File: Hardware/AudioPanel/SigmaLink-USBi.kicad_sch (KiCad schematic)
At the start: 33 parts, among them J28 Program, J32 Target, U68 74LVC2G66, U70 TPS2051B, U71 24LC512, U72 MAX809, U73 CY7C68013A-56, Y9 24MHz

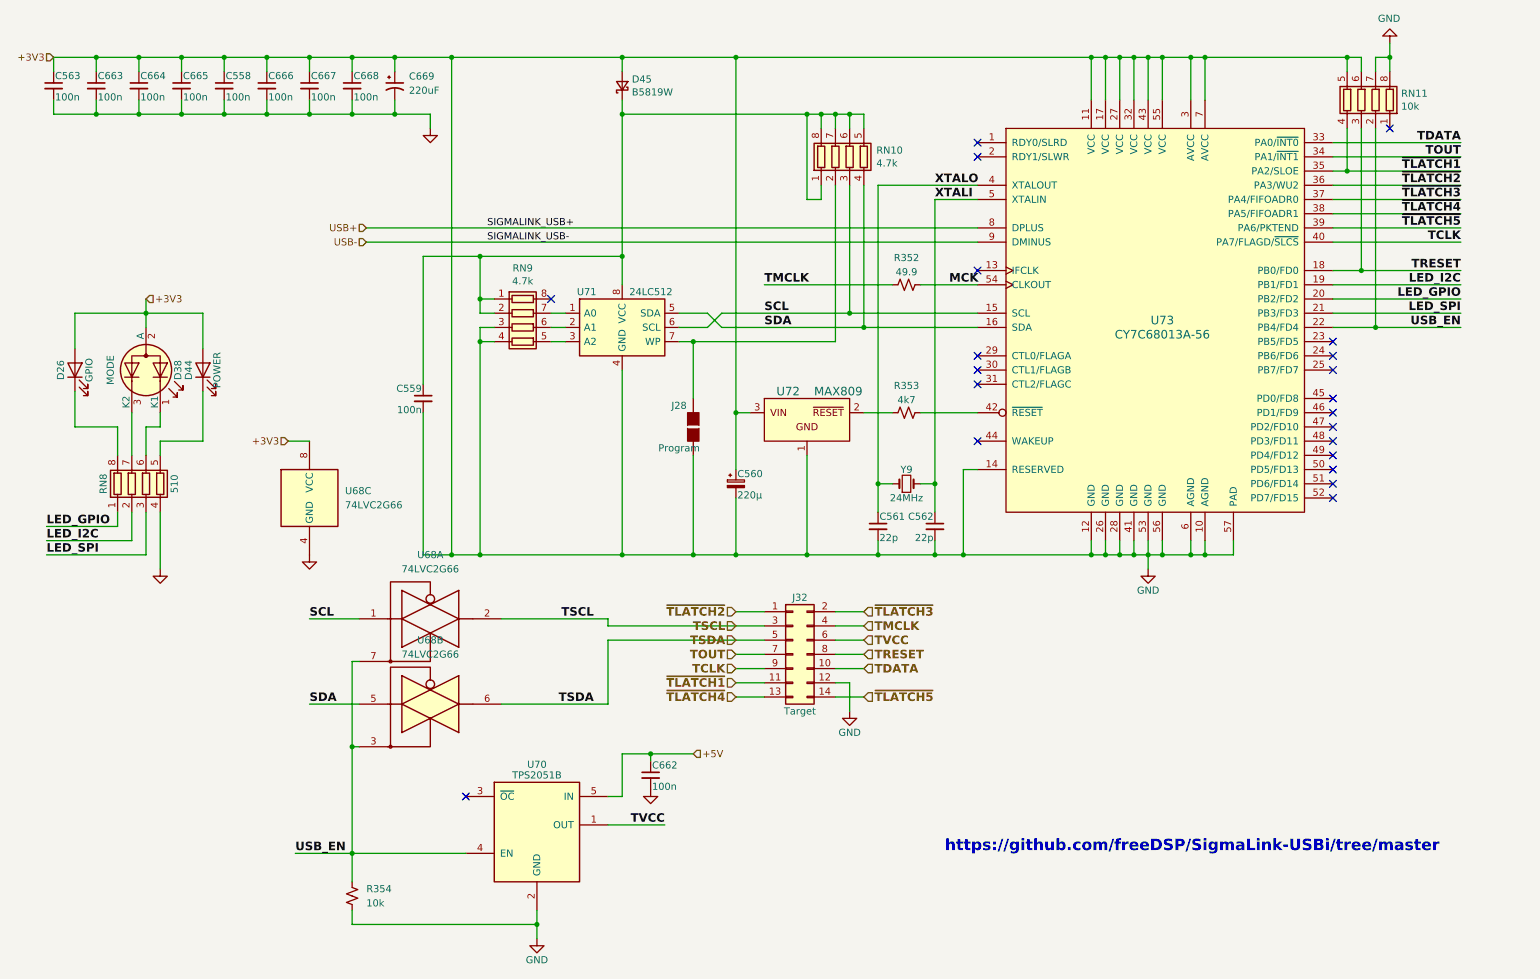
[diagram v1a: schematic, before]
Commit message: Realized that I need to rethink how I'm going to mix the radio audio with the stereo audio
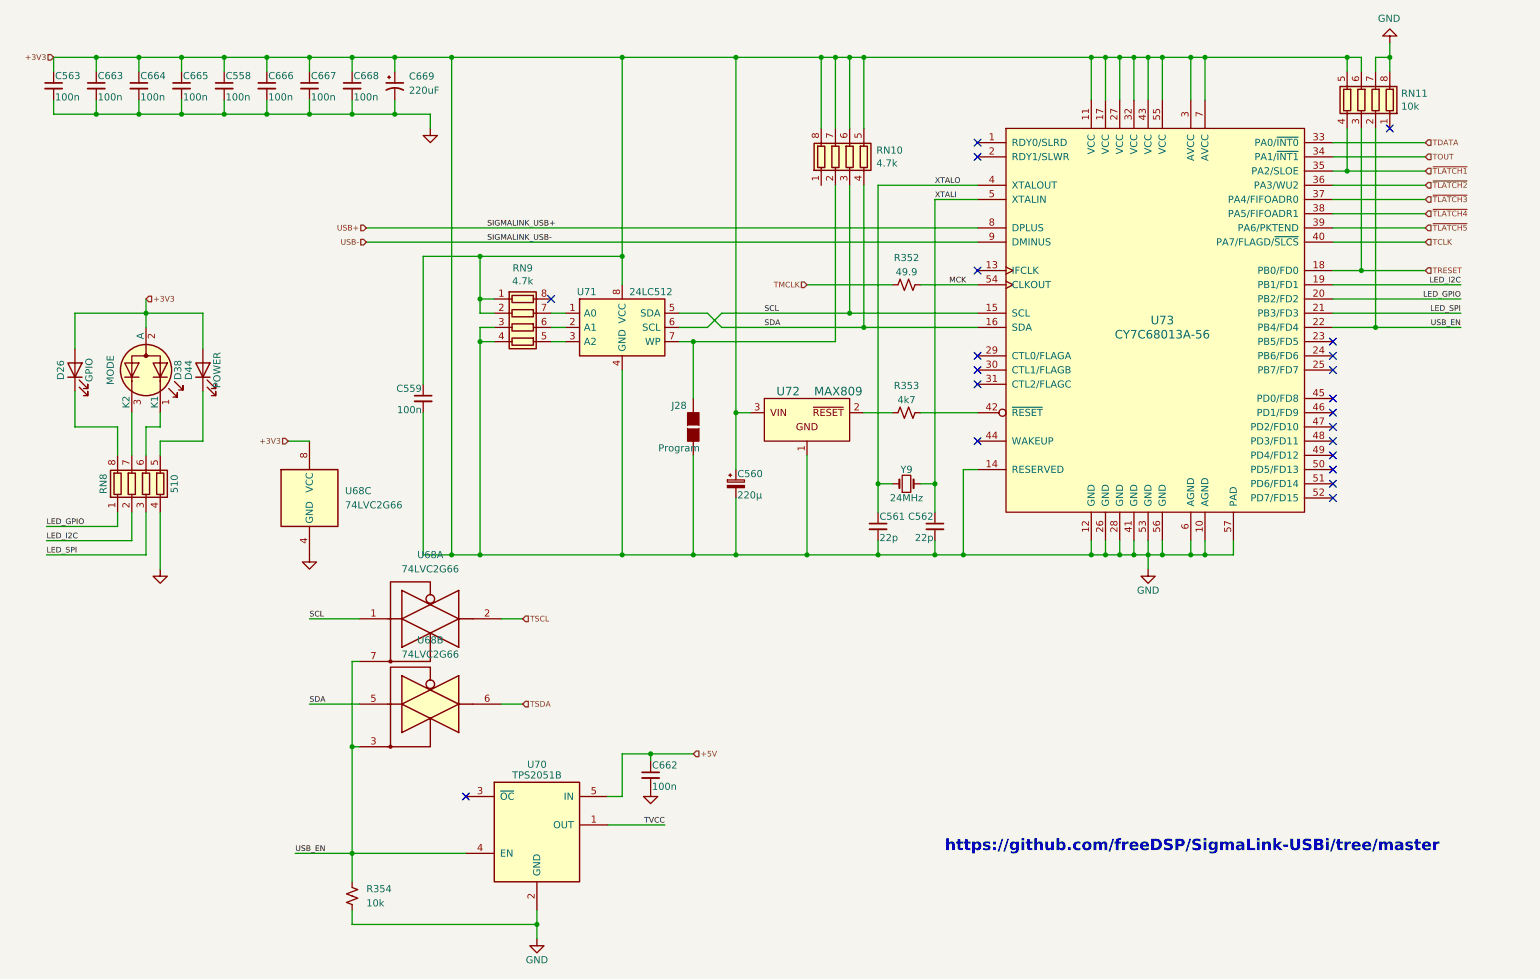
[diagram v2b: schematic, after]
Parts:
- removed D45: B5819W, Diode_SMD:D_SOD-123, symbol Device:D_Schottky_Small
- removed J32: Target, Connector_IDC:IDC-Header_2x07_P2.54mm_Horizontal, symbol Connector_Generic:Conn_02x07_Odd_Even
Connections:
- net GND: now also C559.1, RN10.5 (R4.2), RN10.6 (R3.2), RN10.7 (R2.2), RN10.8 (R1.2), RN9.1 (R1.1), RN9.2 (R2.1), U71.8 (VCC)
- now unconnected: RN10.1 (R1.1)

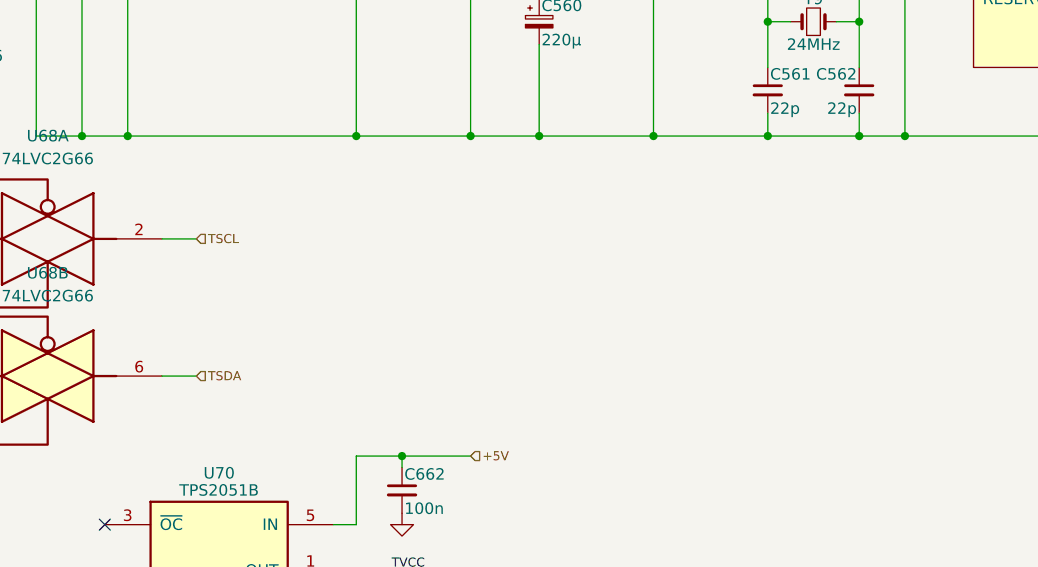
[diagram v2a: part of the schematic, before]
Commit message: Added MT8816 for audio switching
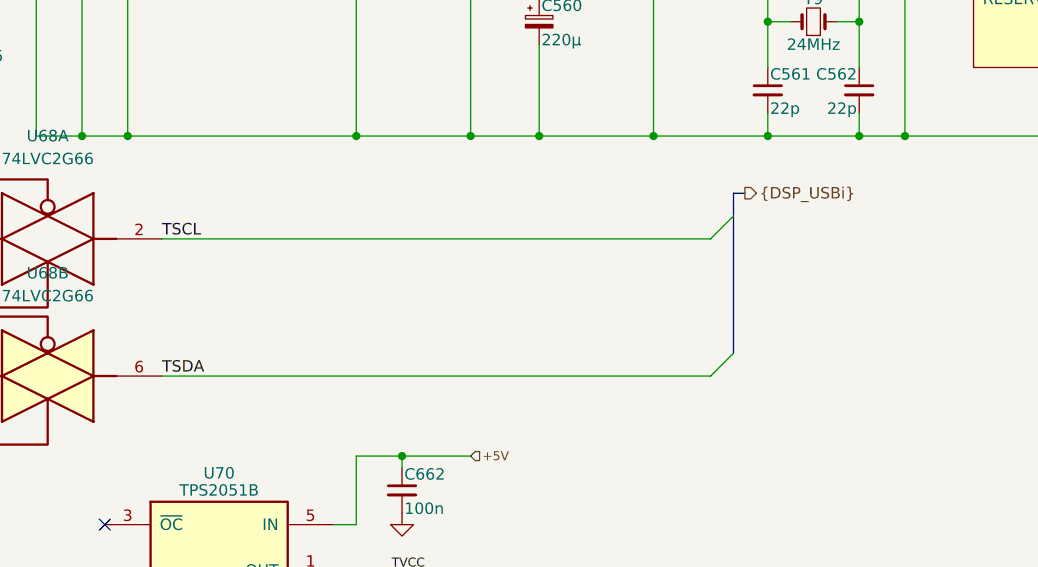
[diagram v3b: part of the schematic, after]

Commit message: Cleaned up stuff, defined more busses
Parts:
- added R458, R460: 33, symbol Device:R_Small_US
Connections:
- net USB+: no longer names the net of U73.8 (DPLUS)
- net USB+: now also R458.2
- net USB-: no longer names the net of U73.9 (DMINUS)
- net USB-: now also R460.2
- new net DSP_SIGMALINK.D+: R458.1
- new net DSP_SIGMALINK.D-: R460.1
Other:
- note added: "https://github.com/freeDSP/DSP_SIGMALINK-USBi/tree/master"
- note removed: "https://github.com/freeDSP/SigmaLink-USBi/tree/master"

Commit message: Removed extraneous pages
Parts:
- renumbered C563 to C759, C663 to C760, C664 to C761, C665 to C762, C558 to C763, C666 to C764, C667 to C765, C668 to C766, C669 to C767, C559 to C768, C662 to C769, C560 to C770, C561 to C771, C562 to C772, D26 to D45, D38 to D46, D44 to D47, J28 to J8, R354 to R446, R352 to R447, R353 to R448, R458 to R459, R460 to R461, RN8 to RN12, RN9 to RN13, RN10 to RN14, RN11 to RN15, U68 to U77, U70 to U78, U71 to U79, U72 to U80, U73 to U81, Y9 to Y10
